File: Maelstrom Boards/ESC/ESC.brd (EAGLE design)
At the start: 101.6 x 101.6 mm, 55 parts, among them P5 MALE1PINHEADER, P6 MALE1PINHEADER, P7 MALE1PINHEADER, P8 MALE1PINHEADER

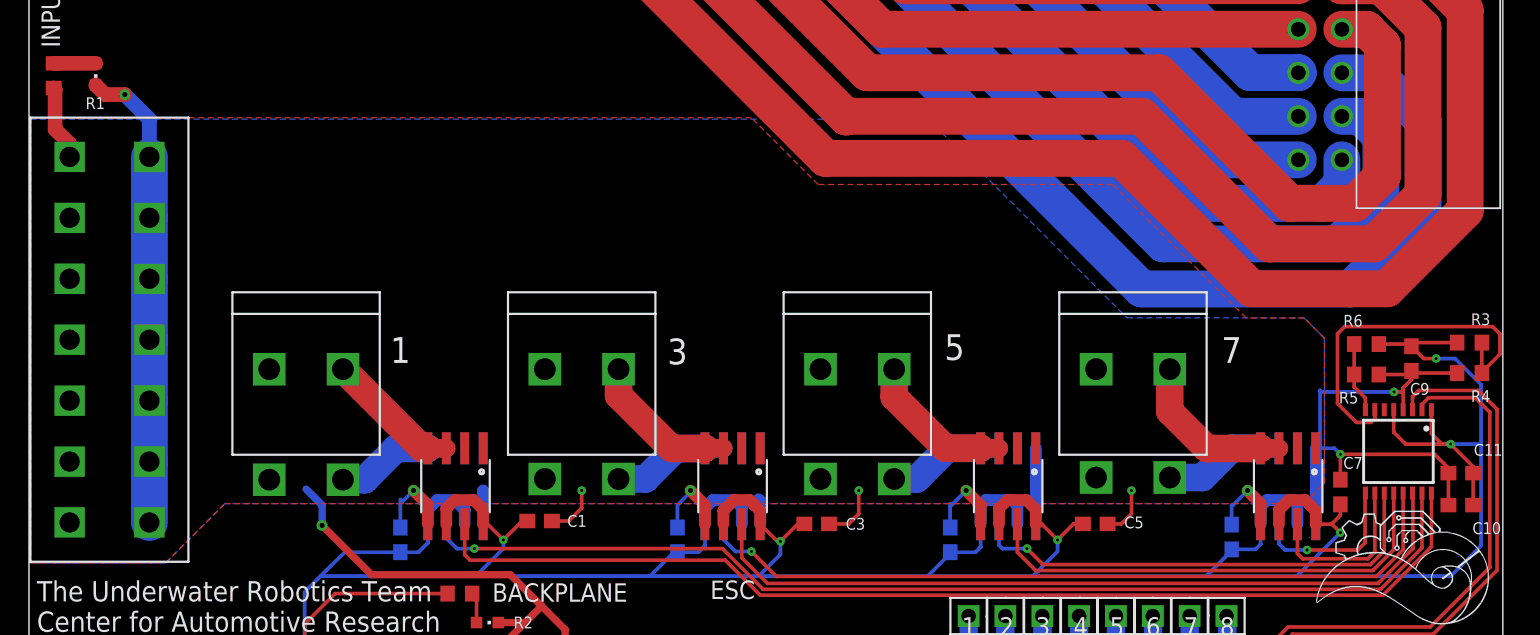
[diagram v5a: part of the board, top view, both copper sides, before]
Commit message: Took out C9, moved some text
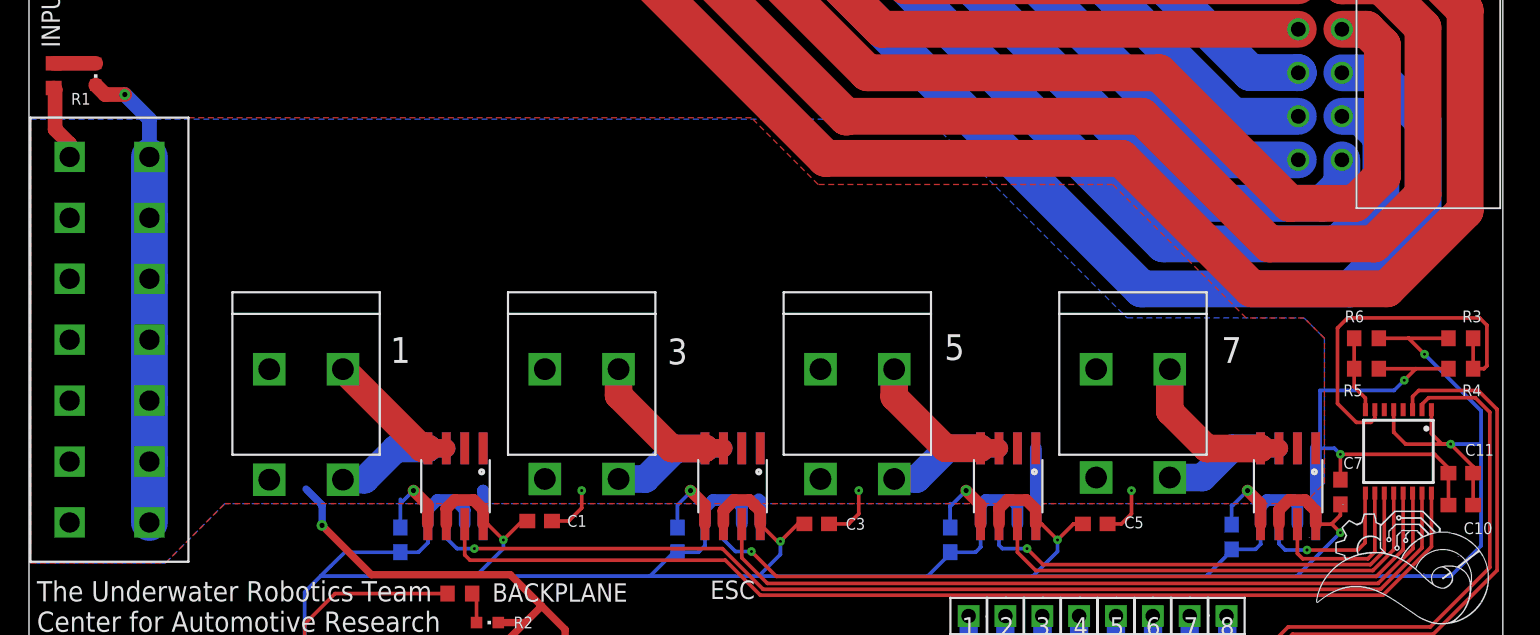
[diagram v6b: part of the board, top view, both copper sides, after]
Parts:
- removed C9: (no value), rcl:C0603
- moved R3 0.67 mm to (98.7, 28.8)
- moved R4 0.67 mm to (98.7, 26.7)
- moved R6 0.40 mm to (92.2, 28.8)
- moved R5 0.40 mm to (92.2, 26.7)
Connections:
- net +3V3: no longer C9.1
- net GND: no longer C9.2
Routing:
- net GND: track 149.0 -> 146.7 mm
- net +3V3: track 236.0 -> 234.6 mm
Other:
- board text removed: "C9"

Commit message: Finishing touches on the ESC board
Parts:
- moved BACKPLANE 1.92 mm to (32.8, 10.7)
- moved R2 0.51 mm to (29.8, 10.7)
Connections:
- removed net +5V: U$1.11, U$1.12, U$1.13, U$1.44, U$1.45, U$1.46
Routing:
- net GND: track 146.7 -> 149.0 mm
- net N$26: track 2.12 -> 1.40 mm
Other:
- board text added: "ESC Board"
- board text removed: "ESC"

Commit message: Final changes before order
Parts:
- added R7: 900, resistor:R0603
- R1: value (none) -> 900
- R2: value (none) -> 5
- R3, R4, R5, R6: value (none) -> 100k
- moved INPUT_POWER 0.90 mm to (5.50, 47.0)
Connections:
- net BALANCED+: now also R7.1
- net N$25: now also R7.2
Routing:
- net N$25: track 2.90 -> 5.50 mm
- net BALANCED+: track 5.21 -> 6.91 mm
- net GND: track 149.0 -> 148.1 mm
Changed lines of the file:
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@@
 <layer number="25" name="tNames" color="7" fill="1" visible="yes" active="yes"/>
 <layer number="26" name="bNames" color="7" fill="1" visible="yes" active="yes"/>
-<layer number="27" name="tValues" color="7" fill="1" visible="yes" active="yes"/>
-<layer number="28" name="bValues" color="7" fill="1" visible="yes" active="yes"/>
+<layer number="27" name="tValues" color="7" fill="1" visible="no" active="yes"/>
+<layer number="28" name="bValues" color="7" fill="1" visible="no" active="yes"/>
 <layer number="29" name="tStop" color="7" fill="3" visible="yes" active="yes"/>
 <layer number="30" name="bStop" color="7" fill="6" visible="yes" active="yes"/>
@@
 <text x="98.8" y="24.8" size="0.8128" layer="25">R4</text>
 <text x="30.7" y="8.8" size="0.8128" layer="25">R2</text>
-<text x="1.1" y="44.5" size="0.8128" layer="25">R1</text>
+<text x="1.8" y="48.9" size="0.8128" layer="25" rot="R90">R1</text>
 <text x="83.2" y="11.3" size="1.27" layer="26" rot="MR0">8</text>
 </plain>
@@
 <element name="P8" library="Male_Header_1Pin" package="MALE1PINHEADER" value="MALE1PINHEADER" x="82.55" y="9.652" smashed="yes" rot="R90"/>
 <element name="U$19" library="14_Pin_Connector_Vert" package="14PIN_VERT" value="14PIN_VERT" x="2.8" y="16.1" smashed="yes"/>
-<element name="R1" library="resistor" library_urn="urn:adsk.eagle:library:348" package="R0603" package3d_urn="urn:adsk.eagle:package:26057/1" value="" x="1.7" y="46.9" smashed="yes" rot="R90">
+<element name="R1" library="resistor" library_urn="urn:adsk.eagle:library:348" package="R0603" package3d_urn="urn:adsk.eagle:package:26057/1" value="900" x="1.7" y="46.9" smashed="yes" rot="R90">
 <attribute name="VALUE" x="3.605" y="46.265" size="1.27" layer="27" rot="R90"/>
 </element>
-<element name="R2" library="resistor" library_urn="urn:adsk.eagle:library:348" package="R0603" package3d_urn="urn:adsk.eagle:package:26057/1" value="" x="29.8" y="10.7" smashed="yes">
+<element name="R2" library="resistor" library_urn="urn:adsk.eagle:library:348" package="R0603" package3d_urn="urn:adsk.eagle:package:26057/1" value="5" x="29.8" y="10.7" smashed="yes">
 <attribute name="VALUE" x="29.165" y="8.795" size="1.27" layer="27"/>
 </element>
@@
 <attribute name="VALUE" x="31.53" y="8.795" size="1.27" layer="27"/>
 </element>
-<element name="INPUT_POWER" library="led" library_urn="urn:adsk.eagle:library:259" package="CHIPLED_0603" package3d_urn="urn:adsk.eagle:package:15822/2" value="" x="4.6" y="47" smashed="yes" rot="R180">
-<attribute name="NAME" x="2.13" y="48.835" size="1.27" layer="25" rot="R90"/>
-<attribute name="VALUE" x="2.695" y="48.27" size="1.27" layer="27" rot="R270"/>
+<element name="INPUT_POWER" library="led" library_urn="urn:adsk.eagle:library:259" package="CHIPLED_0603" package3d_urn="urn:adsk.eagle:package:15822/2" value="" x="5.5" y="47" smashed="yes" rot="R180">
+<attribute name="NAME" x="18.065" y="50.03" size="1.27" layer="25" rot="R180"/>
+<attribute name="VALUE" x="3.595" y="48.27" size="1.27" layer="27" rot="R270"/>
 </element>
 <element name="2CONNECT" library="Screw_Terminals" package="1711725" value="1711725" x="19.1" y="19.05" smashed="yes" rot="MR0"/>
@@
 <element name="4C" library="ACS722" package="SOIC-8" value="ACS722" x="48.5" y="18.6" smashed="yes" rot="MR180"/>
 <element name="U$24" library="ADC128D818" package="TSSOP-16" value="ADC128D818" x="94.4" y="21" smashed="yes" rot="R270"/>
-<element name="R3" library="resistor" library_urn="urn:adsk.eagle:library:348" package="R0603" package3d_urn="urn:adsk.eagle:package:26057/1" value="" x="98.7" y="28.8" smashed="yes">
+<element name="R3" library="resistor" library_urn="urn:adsk.eagle:library:348" package="R0603" package3d_urn="urn:adsk.eagle:package:26057/1" value="100k" x="98.7" y="28.8" smashed="yes">
 <attribute name="VALUE" x="98.065" y="26.895" size="1.27" layer="27"/>
 </element>
-<element name="R4" library="resistor" library_urn="urn:adsk.eagle:library:348" package="R0603" package3d_urn="urn:adsk.eagle:package:26057/1" value="" x="98.7" y="26.7" smashed="yes" rot="R180">
+<element name="R4" library="resistor" library_urn="urn:adsk.eagle:library:348" package="R0603" package3d_urn="urn:adsk.eagle:package:26057/1" value="100k" x="98.7" y="26.7" smashed="yes" rot="R180">
 <attribute name="VALUE" x="99.335" y="28.605" size="1.27" layer="27" rot="R180"/>
 </element>
-<element name="R5" library="resistor" library_urn="urn:adsk.eagle:library:348" package="R0603" package3d_urn="urn:adsk.eagle:package:26057/1" value="" x="92.2" y="26.7" smashed="yes">
+<element name="R5" library="resistor" library_urn="urn:adsk.eagle:library:348" package="R0603" package3d_urn="urn:adsk.eagle:package:26057/1" value="100k" x="92.2" y="26.7" smashed="yes">
 <attribute name="VALUE" x="91.565" y="24.795" size="1.27" layer="27"/>
 </element>
-<element name="R6" library="resistor" library_urn="urn:adsk.eagle:library:348" package="R0603" package3d_urn="urn:adsk.eagle:package:26057/1" value="" x="92.2" y="28.8" smashed="yes" rot="R180">
+<element name="R6" library="resistor" library_urn="urn:adsk.eagle:library:348" package="R0603" package3d_urn="urn:adsk.eagle:package:26057/1" value="100k" x="92.2" y="28.8" smashed="yes" rot="R180">
 <attribute name="VALUE" x="92.835" y="30.705" size="1.27" layer="27" rot="R180"/>
 </element>
@@
 <attribute name="SPICEPREFIX" value="C" x="98.7" y="19.5" size="1.778" layer="27" display="off"/>
 </element>
+<element name="R7" library="resistor" library_urn="urn:adsk.eagle:library:348" package="R0603" package3d_urn="urn:adsk.eagle:package:26057/1" value="900" x="3.4" y="46.9" smashed="yes" rot="R90">
+<attribute name="NAME" x="3.865" y="48.665" size="1.27" layer="25" rot="R90"/>
+<attribute name="VALUE" x="5.305" y="46.265" size="1.27" layer="27" rot="R90"/>
+</element>
 </elements>
 <signals>
@@
 <wire x1="6.6" y1="45.6" x2="8.3" y2="43.9" width="1.016" layer="16"/>
 <wire x1="8.3" y1="43.9" x2="8.3" y2="41.3" width="1.016" layer="16"/>
-<wire x1="4.6" y1="46.25" x2="5.25" y2="45.6" width="1.016" layer="1"/>
-<wire x1="5.25" y1="45.6" x2="6.6" y2="45.6" width="1.016" layer="1"/>
+<wire x1="5.5" y1="46.25" x2="6.15" y2="45.6" width="1.016" layer="1"/>
+<wire x1="6.15" y1="45.6" x2="6.6" y2="45.6" width="1.016" layer="1"/>
 <contactref element="8C" pad="GND"/>
 <contactref element="C11" pad="1"/>
@@
 <wire x1="1.8" y1="43.2" x2="1.8" y2="45.95" width="1.016" layer="1"/>
 <wire x1="1.8" y1="45.95" x2="1.7" y2="46.05" width="1.016" layer="1"/>
+<contactref element="R7" pad="1"/>
+<wire x1="1.7" y1="46.05" x2="3.4" y2="46.05" width="0.508" layer="1"/>
 </signal>
 <signal name="PWM_1">
@@
 <contactref element="R1" pad="2"/>
 <contactref element="INPUT_POWER" pad="A"/>
-<wire x1="1.7" y1="47.75" x2="4.6" y2="47.75" width="1.016" layer="1"/>
+<wire x1="1.7" y1="47.75" x2="5.5" y2="47.75" width="1.016" layer="1"/>
+<contactref element="R7" pad="2"/>
+<wire x1="3.4" y1="47.75" x2="1.7" y2="47.75" width="0.1524" layer="1"/>
 </signal>
 <signal name="N$26">
